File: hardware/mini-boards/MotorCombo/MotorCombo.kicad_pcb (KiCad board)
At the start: 2 copper layers, 26 parts, among them J1 JST_2mm_3, J2 JST_2mm_3, J3 JST_2mm_3, J4 JST_2mm_3, J5 JST_2mm_3, J6 JST_2mm_3, J7 Conn_01x02, J8 Screw_Terminal_01x05, U1 PC817, U2 ESP-01v090

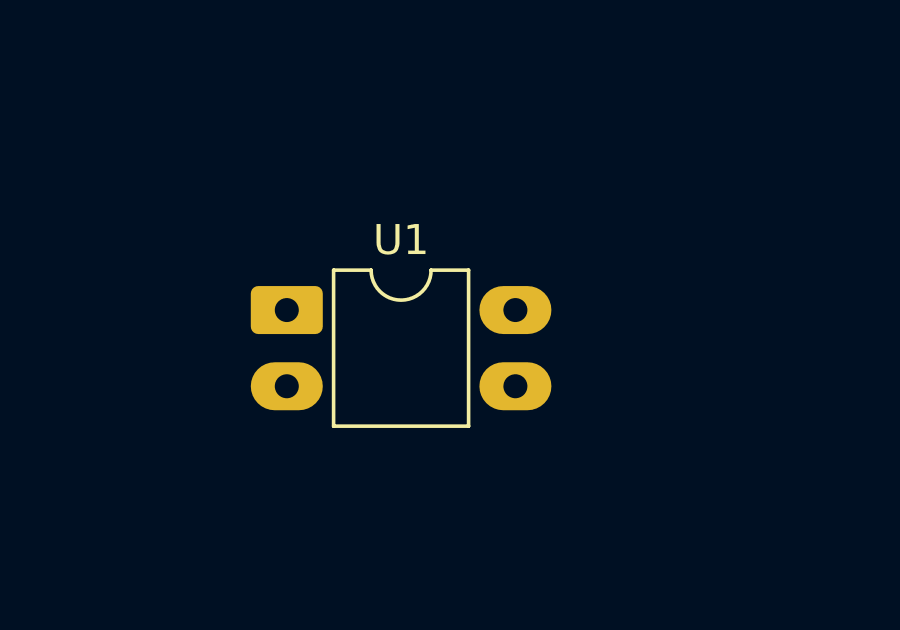
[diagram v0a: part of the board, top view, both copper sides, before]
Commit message: MotorCombo THT: eigenes Board-Projekt mit Gerber-Dateien
Die THT-Variante des MotorCombo-Miniboards liegt jetzt als eigenes
KiCad-Projekt in hardware/mini-boards/MotorCombo_THT/ — inklusive
fertigungsfertiger Gerber-Dateien und Netzliste.

- .gitignore: redundante Backup-Regeln entfernt, **/*-backups/ deckt sie ab
- MotorCombo.kicad_pcb aktualisiert

Co-Authored-By: Claude Opus 4.8 <noreply@anthropic.com>
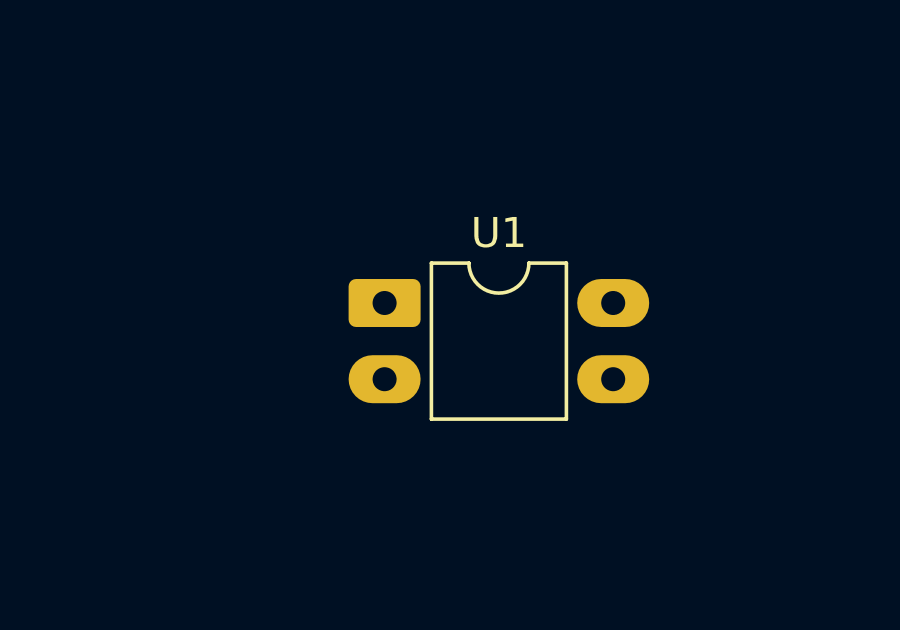
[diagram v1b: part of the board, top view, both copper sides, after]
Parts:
- moved U1 3.27 mm to (129.2, 45.2)
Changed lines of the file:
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@@
 	(footprint "Package_DIP:DIP-4_W7.62mm_LongPads"
 		(layer "F.Cu")
-		(at 125.93 45.46)
+		(at 129.19 45.225)
 		(descr "4-lead though-hole mounted DIP package, row spacing 7.62mm (300 mils), LongPads")
 		(tags "THT DIP DIL PDIP 2.54mm 7.62mm 300mil LongPads")
